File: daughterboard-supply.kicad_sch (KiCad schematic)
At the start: 20 parts, among them J9 39281103, U15 AP62301WU-7, U4 AP62301WU-7

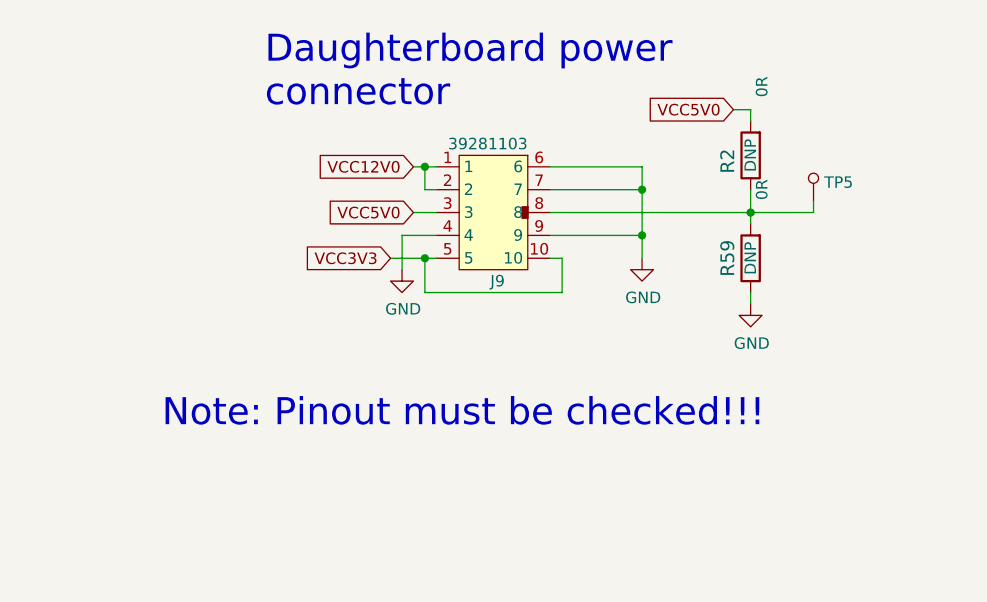
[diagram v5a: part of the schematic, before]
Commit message: Added all changes proposed in first review of the board
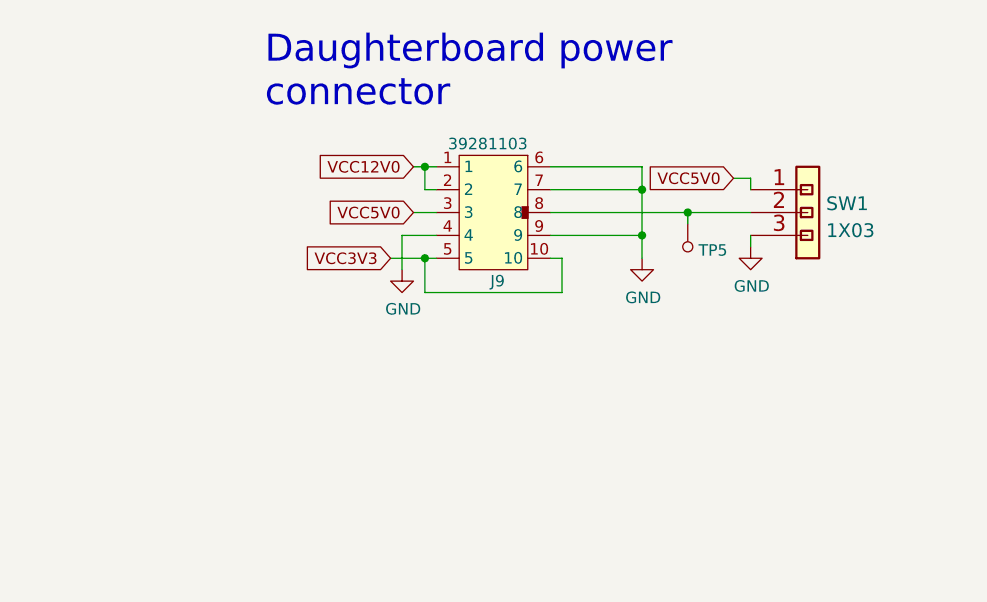
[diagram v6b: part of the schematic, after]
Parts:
- removed R2, R59: R_0R_0402, d1600e-psu-breakout-board-footprints:0402-res, symbol d1600e-psu-breakout-board:R_0R_0402
- added SW1: 1X03, antmicro-footprints:MH_1X03_2.54, symbol antmicroRectangularConnectorsHeadersMalePins:1X03
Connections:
- net GND: now also SW1.3
- net VCC5V0: now also SW1.1
- net at J9.8, TP5.1: now also SW1.2
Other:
- note removed: "Note: Pinout must be checked!!!"
- moved on the sheet: TP5
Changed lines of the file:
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@@
   (junction (at 295.275 114.935) (diameter 0) (color 0 0 0 0)
   )
+  (junction (at 300.355 117.475) (diameter 0) (color 0 0 0 0)
+  )
   (junction (at 168.91 169.545) (diameter 0) (color 0 0 0 0)
   )
@@
   (junction (at 121.92 169.545) (diameter 0) (color 0 0 0 0)
   )
-  (junction (at 307.34 117.475) (diameter 0) (color 0 0 0 0)
-  )
   (junction (at 193.04 169.545) (diameter 0) (color 0 0 0 0)
   )
@@
     (stroke (width 0) (type default) (color 0 0 0 0))
   )
+  (wire (pts (xy 300.355 118.745) (xy 300.355 117.475))
+    (stroke (width 0) (type default) (color 0 0 0 0))
+  )
   (wire (pts (xy 271.145 122.555) (xy 272.415 122.555))
     (stroke (width 0) (type default) (color 0 0 0 0))
   )
-  (wire (pts (xy 307.34 107.315) (xy 307.34 106.045))
+  (wire (pts (xy 307.34 114.935) (xy 307.34 113.665))
     (stroke (width 0) (type default) (color 0 0 0 0))
   )
@@
     (stroke (width 0) (type default) (color 0 0 0 0))
   )
+  (wire (pts (xy 300.355 117.475) (xy 307.34 117.475))
+    (stroke (width 0) (type default) (color 0 0 0 0))
+  )
   (wire (pts (xy 122.555 135.255) (xy 122.555 128.905))
     (stroke (width 0) (type default) (color 0 0 0 0))
@@
     (stroke (width 0) (type default) (color 0 0 0 0))
   )
-  (wire (pts (xy 307.34 114.935) (xy 307.34 117.475))
-    (stroke (width 0) (type default) (color 0 0 0 0))
-  )
-  (wire (pts (xy 314.325 117.475) (xy 307.34 117.475))
-    (stroke (width 0) (type default) (color 0 0 0 0))
-  )
-  (wire (pts (xy 307.34 126.365) (xy 307.34 127.635))
-    (stroke (width 0) (type default) (color 0 0 0 0))
-  )
-  (wire (pts (xy 307.34 117.475) (xy 307.34 118.745))
+  (wire (pts (xy 307.34 120.015) (xy 307.34 121.285))
     (stroke (width 0) (type default) (color 0 0 0 0))
   )
@@
     (stroke (width 0) (type default) (color 0 0 0 0))
   )
-  (wire (pts (xy 314.325 116.205) (xy 314.325 117.475))
-    (stroke (width 0) (type default) (color 0 0 0 0))
-  )
   (wire (pts (xy 168.91 169.545) (xy 171.45 169.545))
     (stroke (width 0) (type default) (color 0 0 0 0))
@@
     (stroke (width 0) (type default) (color 0 0 0 0))
   )
-  (wire (pts (xy 307.34 106.045) (xy 305.435 106.045))
+  (wire (pts (xy 307.34 113.665) (xy 305.435 113.665))
     (stroke (width 0) (type default) (color 0 0 0 0))
   )
@@
     (stroke (width 0) (type default) (color 0 0 0 0))
   )
-  (wire (pts (xy 285.115 117.475) (xy 307.34 117.475))
+  (wire (pts (xy 285.115 117.475) (xy 300.355 117.475))
     (stroke (width 0) (type default) (color 0 0 0 0))
   )
@@
     (effects (font (size 1.27 1.27)) (justify left bottom))
   )
-  (text "Note: Pinout must be checked!!!" (at 241.935 141.605 0)
-    (effects (font (size 3 3)) (justify left bottom))
-  )
   (global_label "VCC3V3" (shape input) (at 212.09 169.545 0) (fields_autoplaced)
     (effects (font (size 1.27 1.27)) (justify left))
@@
     )
   )
-  (global_label "VCC5V0" (shape input) (at 305.435 106.045 180) (fields_autoplaced)
+  (global_label "VCC5V0" (shape input) (at 305.435 113.665 180) (fields_autoplaced)
     (effects (font (size 1.27 1.27)) (justify right))
-    (property "Intersheet References" "${INTERSHEET_REFS}" (id 0) (at 71.755 48.895 0)
+    (property "Intersheet References" "${INTERSHEET_REFS}" (id 0) (at 71.755 56.515 0)
       (effects (font (size 1.27 1.27)) hide)
     )
@@
     (pin "2")
   )
-  (symbol (lib_id "d1600e-psu-breakout-board:R_0R_0402") (at 307.34 111.125 90) (unit 1)
+  (symbol (lib_id "d1600e-psu-breakout-board:GND") (at 307.34 121.285 0) (unit 1)
     (in_bom yes) (on_board yes)
-    (property "Reference" "R2" (id 0) (at 304.8 111.76 0)
-      (effects (font (size 1.524 1.524)))
-    )
-    (property "Value" "R_0R_0402" (id 1) (at 311.15 111.125 0)
-      (effects (font (size 1.524 1.524)) hide)
-    )
-    (property "Footprint" "d1600e-psu-breakout-board-footprints:0402-res" (id 2) (at 302.26 106.045 0)
-      (effects (font (size 1.524 1.524)) (justify left) hide)
-    )
-    (property "Datasheet" "" (id 3) (at 307.34 111.125 0)
+    (property "Reference" "#PWR0135" (id 0) (at 307.34 127.635 0)
       (effects (font (size 1.27 1.27)) hide)
     )
-    (property "Manufacturer" "PANASONIC" (id 4) (at 297.18 106.045 0)
-      (effects (font (size 1.524 1.524)) (justify left) hide)
-    )
-    (property "MPN" "ERJ2GE0R00X" (id 5) (at 299.72 106.045 0)
-      (effects (font (size 1.524 1.524)) (justify left) hide)
-    )
-    (property "Val" "0R" (id 6) (at 308.61 103.505 0))
-    (property "DNP" "DNP" (id 7) (at 307.34 111.125 0))
-    (pin "1")
-    (pin "2")
-  )
-  (symbol (lib_id "d1600e-psu-breakout-board:GND") (at 307.34 127.635 0) (unit 1)
-    (in_bom yes) (on_board yes)
-    (property "Reference" "#PWR0135" (id 0) (at 307.34 133.985 0)
+    (property "Value" "GND" (id 1) (at 307.467 125.6792 0))
+    (property "Footprint" "d1600e-psu-breakout-board-footprints:" (id 2) (at 307.34 121.285 0)
       (effects (font (size 1.27 1.27)) hide)
     )
-    (property "Value" "GND" (id 1) (at 307.467 132.0292 0))
-    (property "Footprint" "d1600e-psu-breakout-board-footprints:" (id 2) (at 307.34 127.635 0)
-      (effects (font (size 1.27 1.27)) hide)
-    )
-    (property "Datasheet" "" (id 3) (at 307.34 127.635 0)
+    (property "Datasheet" "" (id 3) (at 307.34 121.285 0)
       (effects (font (size 1.27 1.27)) hide)
     )
     (pin "1")
   )
-  (symbol (lib_id "d1600e-psu-breakout-board:R_0R_0402") (at 307.34 122.555 90) (unit 1)
-    (in_bom yes) (on_board yes)
-    (property "Reference" "R59" (id 0) (at 304.8 122.555 0)
-      (effects (font (size 1.524 1.524)))
+  (symbol (lib_id "antmicroRectangularConnectorsHeadersMalePins:1X03") (at 312.42 117.475 0) (unit 1)
+    (in_bom yes) (on_board yes) (fields_autoplaced)
+    (property "Reference" "SW1" (id 0) (at 315.722 116.4988 0)
+      (effects (font (size 1.524 1.524)) (justify left))
+    )
+    (property "Value" "1X03" (id 1) (at 315.722 119.4922 0)
+      (effects (font (size 1.524 1.524)) (justify left))
     )
-    (property "Value" "R_0R_0402" (id 1) (at 311.15 122.555 0)
+    (property "Footprint" "antmicro-footprints:MH_1X03_2.54" (id 2) (at 322.58 126.365 0)
       (effects (font (size 1.524 1.524)) hide)
     )
-    (property "Footprint" "d1600e-psu-breakout-board-footprints:0402-res" (id 2) (at 302.26 117.475 0)
-      (effects (font (size 1.524 1.524)) (justify left) hide)
+    (property "Datasheet" "https://www.we-online.com/catalog/datasheet/61300311121.pdf" (id 3) (at 312.42 117.475 0)
+      (effects (font (size 1.524 1.524)) hide)
     )
-    (property "Datasheet" "" (id 3) (at 307.34 122.555 0)
+    (property "MPN" "61300311121" (id 4) (at 308.61 128.905 0)
       (effects (font (size 1.27 1.27)) hide)
     )
-    (property "Manufacturer" "PANASONIC" (id 4) (at 297.18 117.475 0)
-      (effects (font (size 1.524 1.524)) (justify left) hide)
-    )
-    (property "MPN" "ERJ2GE0R00X" (id 5) (at 299.72 117.475 0)
-      (effects (font (size 1.524 1.524)) (justify left) hide)
+    (property "Manufacturer" "Wurth Elektronik" (id 5) (at 309.88 131.445 0)
+      (effects (font (size 1.27 1.27)) hide)
     )
-    (property "Val" "0R" (id 6) (at 308.61 114.935 0))
-    (property "DNP" "DNP" (id 7) (at 307.34 122.555 0))
     (pin "1")
     (pin "2")
+    (pin "3")
   )
   (symbol (lib_id "d1600e-psu-breakout-board:GND") (at 295.275 122.555 0) (unit 1)
@@
     (pin "1")
   )
-  (symbol (lib_id "antmicroTestPoints:TP_SMD1MM") (at 314.325 113.665 180) (unit 1)
+  (symbol (lib_id "antmicroTestPoints:TP_SMD1MM") (at 300.355 121.285 0) (unit 1)
     (in_bom yes) (on_board yes) (fields_autoplaced)
-    (property "Reference" "TP5" (id 0) (at 315.5188 114.1369 0)
-      (effects (font (size 1.27 1.27)) (justify right))
+    (property "Reference" "TP5" (id 0) (at 301.5488 121.6807 0)
+      (effects (font (size 1.27 1.27)) (justify left))
     )
-    (property "Value" "TP_SMD1MM" (id 1) (at 314.325 111.125 0)
+    (property "Value" "TP_SMD1MM" (id 1) (at 300.355 123.825 0)
       (effects (font (size 1.27 1.27)) hide)
     )
-    (property "Footprint" "antmicro-footprints:Testpoint_smd_1mm" (id 2) (at 309.245 118.745 0)
+    (property "Footprint" "antmicro-footprints:Testpoint_smd_1mm" (id 2) (at 305.435 116.205 0)
       (effects (font (size 1.524 1.524)) (justify left) hide)
     )
-    (property "Datasheet" "" (id 3) (at 309.245 121.285 0)
+    (property "Datasheet" "" (id 3) (at 305.435 113.665 0)
       (effects (font (size 1.524 1.524)) (justify left) hide)
     )
